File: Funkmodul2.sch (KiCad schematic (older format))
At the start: 54 parts, among them Q10 AO3414, Q18 AO3414, Q9 SSM3J334RLFTR-ND, U6 MC74HC4538A, U7 MAX892, U8 ATMEGA128-16AU, Y2 407F39D007M3728

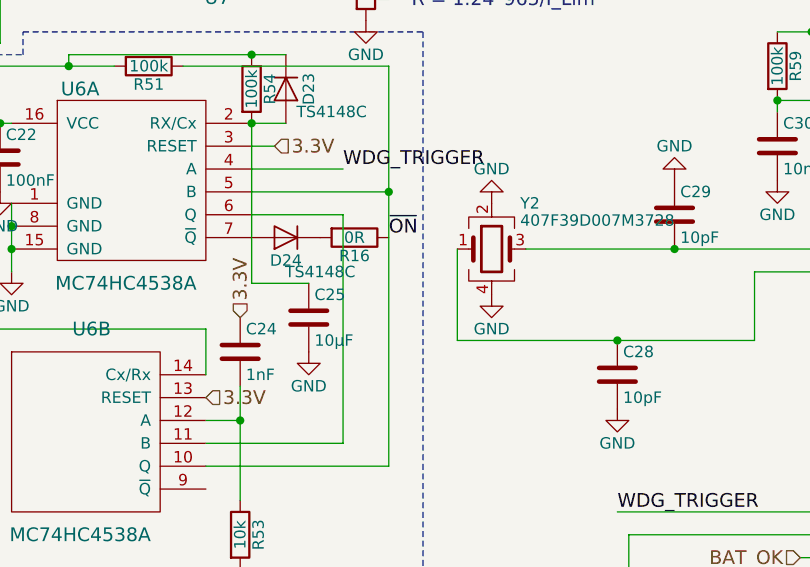
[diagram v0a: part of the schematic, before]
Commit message: Bugfix for external watchdog circuit
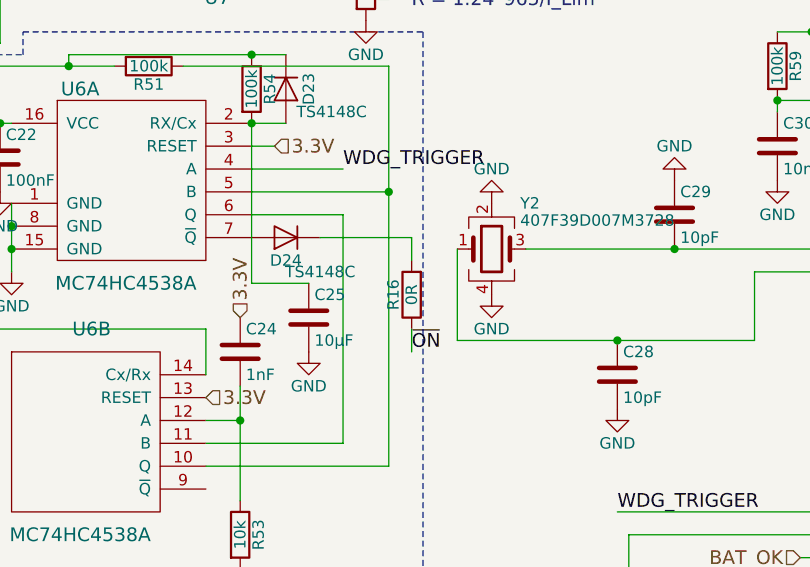
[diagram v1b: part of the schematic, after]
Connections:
- net ~ON~: no longer R51.1, U6.10 (Q), U6.5 (B)
- new net: R51.1, U6.10 (Q), U6.5 (B)
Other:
- moved on the sheet: R16
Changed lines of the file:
@@
 LIBS:contrib
 LIBS:valves
+LIBS:nxp-ic
+LIBS:7400-ic
 LIBS:cubesatFunkmodul-cache
 LIBS:funkmodul
+LIBS:CubeSat-Bus-1
+LIBS:CubeSat-Bus-2
 LIBS:disco-con
 LIBS:fiducial
@@
 Text Label 2000 1250 0    60   ~ 0
 ~ON~
-Text Label 3300 2600 0    60   ~ 0
+Text Label 3400 3100 0    60   ~ 0
 ~ON~
 Text Label 3100 2300 0    60   ~ 0
@@
 L R R16
 U 1 1 5A0FAB4F
-P 3150 2600
-F 0 "R16" V 3230 2600 50  0000 C CNN
-F 1 "0R" V 3150 2600 50  0000 C CNN
-F 2 "Resistors_SMD:R_0805_HandSoldering" V 3080 2600 50  0001 C CNN
-F 3 "" H 3150 2600 50  0001 C CNN
-	1    3150 2600
-	0    1    1    0
-$EndComp
+P 3400 2850
+F 0 "R16" V 3480 2850 50  0000 C CNN
+F 1 "0R" V 3400 2850 50  0000 C CNN
+F 2 "Resistors_SMD:R_0805_HandSoldering" V 3330 2850 50  0001 C CNN
+F 3 "" H 3400 2850 50  0001 C CNN
+	1    3400 2850
+	-1   0    0    1
+$EndComp
+Wire Wire Line
+	3400 3100 3400 3000
+Wire Wire Line
+	3000 2600 3400 2600
+Wire Wire Line
+	3400 2600 3400 2700
 $EndSCHEMATC

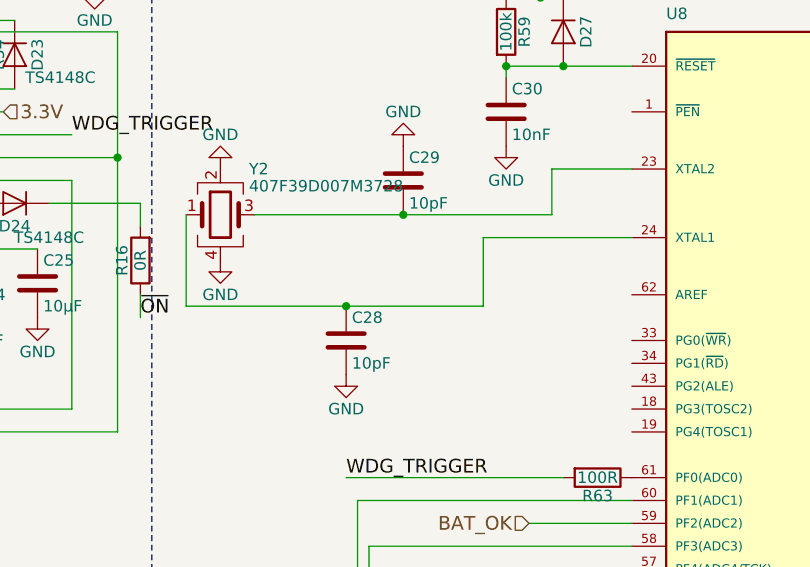
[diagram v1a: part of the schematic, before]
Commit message: Changes to get in production
- Adds connector outlines to component scheme
- Changes crystalcapacitors to 15pF
- Regenerated top and bottom component scheme
- Adds formated BOM list for betalayout
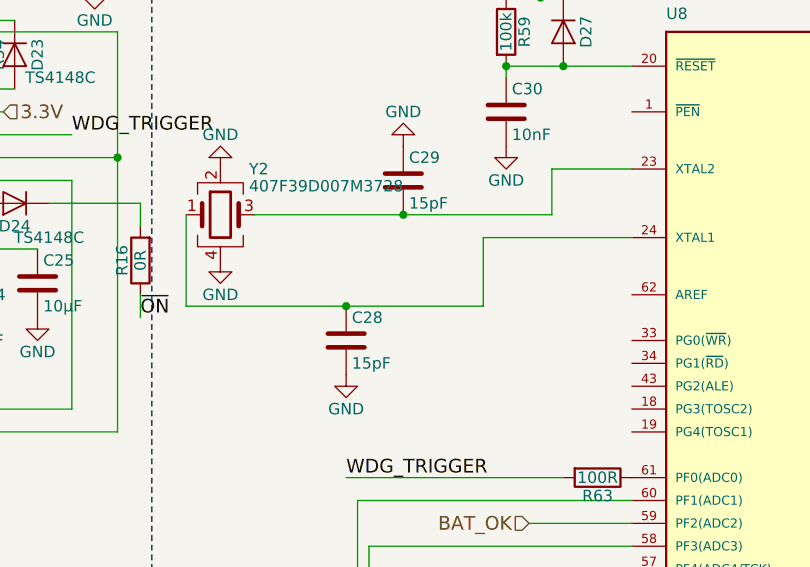
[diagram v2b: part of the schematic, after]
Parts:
- C28, C29: value 10pF -> 15pF
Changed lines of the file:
@@
 P 4300 3200
 F 0 "C28" H 4325 3300 50  0000 L CNN
-F 1 "10pF" H 4325 3100 50  0000 L CNN
+F 1 "15pF" H 4325 3100 50  0000 L CNN
 F 2 "Capacitors_SMD:C_0603_HandSoldering" H 4338 3050 50  0001 C CNN
 F 3 "" H 4300 3200 50  0001 C CNN
@@
 P 4550 2500
 F 0 "C29" H 4575 2600 50  0000 L CNN
-F 1 "10pF" H 4575 2400 50  0000 L CNN
+F 1 "15pF" H 4575 2400 50  0000 L CNN
 F 2 "Capacitors_SMD:C_0603_HandSoldering" H 4588 2350 50  0001 C CNN
 F 3 "" H 4550 2500 50  0001 C CNN

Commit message: Converted to new kicad version
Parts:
- C21, C22, C23, C24, C25, C26, C27, C28, C29, C30, C31, C32, C33, C42: symbol C -> cubesatFunkmodul-rescue:C
- D19, D20, D21, D22, D23, D24, D25, D26, D27, D31, D32: symbol D -> cubesatFunkmodul-rescue:D
- D28: symbol D_Zener -> cubesatFunkmodul-rescue:D_Zener
- L3: symbol Ferrite_Bead -> cubesatFunkmodul-rescue:Ferrite_Bead
- Q10, Q18: symbol Q_NMOS_DGS -> cubesatFunkmodul-rescue:Q_NMOS_DGS
- Q9: symbol Q_PMOS_SGD -> cubesatFunkmodul-rescue:Q_PMOS_SGD
- R16, R46, R47, R48, R49, R50, R51, R52, R53, R54, R55, R56, R57, R58, R59, R63, R95, R96, R97, R98: symbol R -> cubesatFunkmodul-rescue:R
- U6: symbol MC74HC4538A -> cubesatFunkmodul-rescue:MC74HC4538A
- U7: symbol MAX892 -> cubesatFunkmodul-rescue:MAX892
- U8: symbol ATMEGA128-16AU -> cubesatFunkmodul-rescue:ATMEGA128-16AU
- Y2: symbol Crystal_GND24 -> cubesatFunkmodul-rescue:Crystal_GND24
